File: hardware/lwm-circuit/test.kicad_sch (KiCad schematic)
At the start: 29 parts, among them J1 Analog, J2 Digital, J4 Micro_SD_Card_Det_Hirose_DM3AT, U1 MCP23017x-x-ML, U2 MCP23017x-x-ML, U3 MCP23017x-x-ML, U4 MCP23017x-x-ML, U5 MCP23017x-x-ML, U6 254

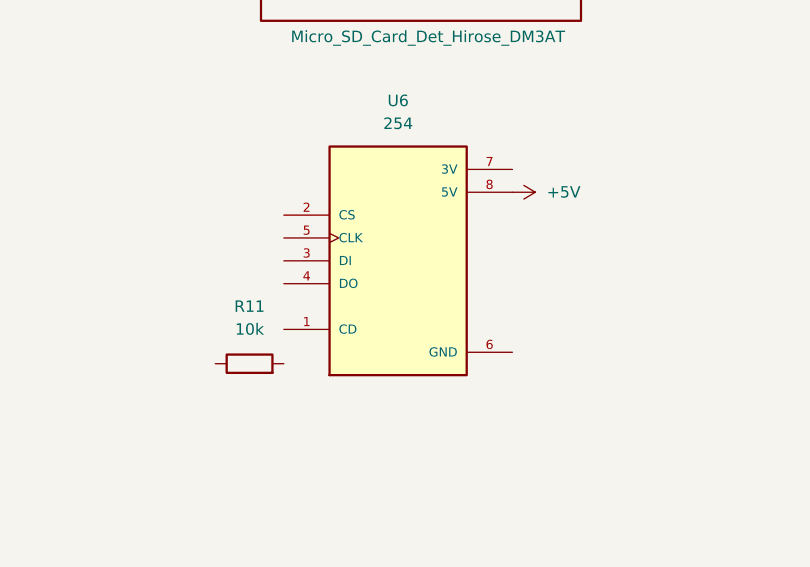
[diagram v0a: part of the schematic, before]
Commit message: rewired sd card
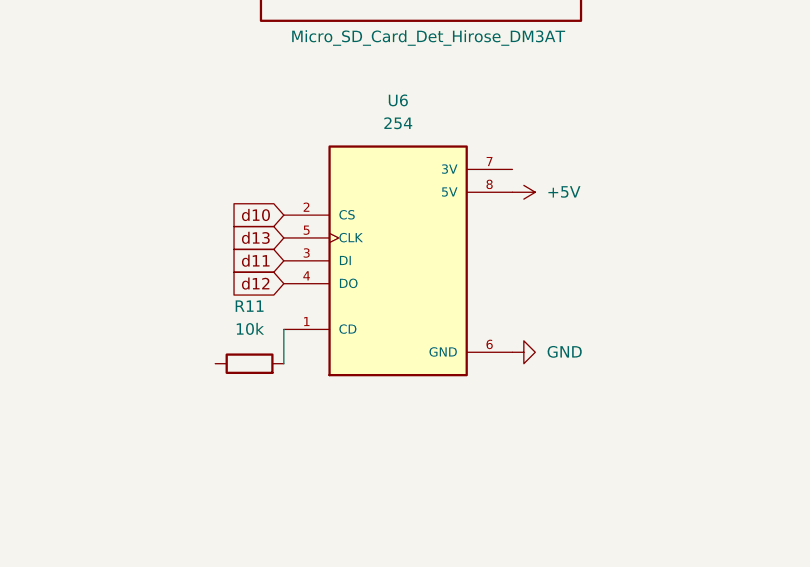
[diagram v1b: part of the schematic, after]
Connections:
- net GND: now also U6.6 (GND)
- net at U6.1 (CD): now also R11.2
- net d10: now reaches U6.2 (CS)
- net d11: now reaches U6.3 (DI)
- net d12: now reaches U6.4 (DO)
- net d13: now reaches U6.5 (CLK)
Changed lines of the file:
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@@
 	(wire
 		(pts
+			(xy 57.15 158.75) (xy 57.15 162.56)
+		)
+		(stroke
+			(width 0)
+			(type default)
+		)
+	)
+	(wire
+		(pts
 			(xy 24.13 20.32) (xy 135.89 20.32)
 		)
@@
 		)
 	)
+	(global_label "d11"
+		(shape input)
+		(at 57.15 151.13 180)
+		(fields_autoplaced yes)
+		(effects
+			(font
+				(size 1.27 1.27)
+			)
+			(justify right)
+		)
+		(property "Intersheetrefs" "${INTERSHEET_REFS}"
+			(at 53.8157 151.13 0)
+			(hide yes)
+			(show_name no)
+			(do_not_autoplace no)
+			(effects
+				(font
+					(size 1.27 1.27)
+				)
+				(justify right)
+			)
+		)
+	)
 	(global_label "R_1_DIAG"
 		(shape output)
@@
 		)
 	)
+	(global_label "d10"
+		(shape input)
+		(at 57.15 146.05 180)
+		(fields_autoplaced yes)
+		(effects
+			(font
+				(size 1.27 1.27)
+			)
+			(justify right)
+		)
+		(property "Intersheetrefs" "${INTERSHEET_REFS}"
+			(at 50.5017 146.05 0)
+			(hide yes)
+			(show_name no)
+			(do_not_autoplace no)
+			(effects
+				(font
+					(size 1.27 1.27)
+				)
+				(justify right)
+			)
+		)
+	)
 	(global_label "R_3_DIR"
 		(shape input)
@@
 		)
 	)
+	(global_label "d13"
+		(shape input)
+		(at 57.15 148.59 180)
+		(fields_autoplaced yes)
+		(effects
+			(font
+				(size 1.27 1.27)
+			)
+			(justify right)
+		)
+		(property "Intersheetrefs" "${INTERSHEET_REFS}"
+			(at 53.8157 148.59 0)
+			(hide yes)
+			(show_name no)
+			(do_not_autoplace no)
+			(effects
+				(font
+					(size 1.27 1.27)
+				)
+				(justify right)
+			)
+		)
+	)
 	(global_label "E_3_DIR"
 		(shape input)
@@
 		)
 	)
+	(global_label "d12"
+		(shape input)
+		(at 57.15 153.67 180)
+		(fields_autoplaced yes)
+		(effects
+			(font
+				(size 1.27 1.27)
+			)
+			(justify right)
+		)
+		(property "Intersheetrefs" "${INTERSHEET_REFS}"
+			(at 50.5017 153.67 0)
+			(hide yes)
+			(show_name no)
+			(do_not_autoplace no)
+			(effects
+				(font
+					(size 1.27 1.27)
+				)
+				(justify right)
+			)
+		)
+	)
 	(global_label "CS"
 		(shape input)
@@
 	)
 	(symbol
+		(lib_id "Device:R")
+		(at 53.34 162.56 90)
+		(unit 1)
+		(body_style 1)
+		(exclude_from_sim no)
+		(in_bom yes)
+		(on_board yes)
+		(in_pos_files yes)
+		(dnp no)
+		(fields_autoplaced yes)
+		(property "Reference" "R11"
+			(at 53.34 156.21 90)
+			(show_name no)
+			(do_not_autoplace no)
+			(effects
+				(font
+					(size 1.27 1.27)
+				)
+			)
+		)
+		(property "Value" "10k"
+			(at 53.34 158.75 90)
+			(show_name no)
+			(do_not_autoplace no)
+			(effects
+				(font
+					(size 1.27 1.27)
+				)
+			)
+		)
+		(property "Footprint" ""
+			(at 53.34 164.338 90)
+			(hide yes)
+			(show_name no)
+			(do_not_autoplace no)
+			(effects
+				(font
+					(size 1.27 1.27)
+				)
+			)
+		)
+		(property "Datasheet" ""
+			(at 53.34 162.56 0)
+			(hide yes)
+			(show_name no)
+			(do_not_autoplace no)
+			(effects
+				(font
+					(size 1.27 1.27)
+				)
+			)
+		)
+		(property "Description" "Resistor"
+			(at 53.34 162.56 0)
+			(hide yes)
+			(show_name no)
+			(do_not_autoplace no)
+			(effects
+				(font
+					(size 1.27 1.27)
+				)
+			)
+		)
+		(pin "1"
+		)
+		(pin "2"
+		)
+		(instances
+			(project "test"
+				(path "/0d35483a-0b12-46cc-b9f2-896fd6831779"
+					(reference "R11")
+					(unit 1)
+				)
+			)
+		)
+	)
+	(symbol
 		(lib_id "Adafruit TMC2209 Stepper Motor Driver-eagle-import:HEADER-1X1070MIL")
 		(at 171.45 210.82 90)
@@
 	)
 	(symbol
-		(lib_id "Device:R")
-		(at 53.34 162.56 90)
-		(unit 1)
-		(body_style 1)
-		(exclude_from_sim no)
-		(in_bom yes)
-		(on_board yes)
-		(in_pos_files yes)
-		(dnp no)
-		(fields_autoplaced yes)
-		(property "Reference" "R11"
-			(at 53.34 156.21 90)
-			(show_name no)
-			(do_not_autoplace no)
-			(effects
-				(font
-					(size 1.27 1.27)
-				)
-			)
-		)
-		(property "Value" "10k"
-			(at 53.34 158.75 90)
-			(show_name no)
-			(do_not_autoplace no)
-			(effects
-				(font
-					(size 1.27 1.27)
-				)
-			)
-		)
-		(property "Footprint" ""
-			(at 53.34 164.338 90)
-			(hide yes)
-			(show_name no)
-			(do_not_autoplace no)
-			(effects
-				(font
-					(size 1.27 1.27)
-				)
-			)
-		)
-		(property "Datasheet" ""
-			(at 53.34 162.56 0)
-			(hide yes)
-			(show_name no)
-			(do_not_autoplace no)
-			(effects
-				(font
-					(size 1.27 1.27)
-				)
-			)
-		)
-		(property "Description" "Resistor"
-			(at 53.34 162.56 0)
-			(hide yes)
-			(show_name no)
-			(do_not_autoplace no)
-			(effects
-				(font
-					(size 1.27 1.27)
-				)
-			)
-		)
-		(pin "1"
-		)
-		(pin "2"
-		)
-		(instances
-			(project "test"
-				(path "/0d35483a-0b12-46cc-b9f2-896fd6831779"
-					(reference "R11")
-					(unit 1)
-				)
-			)
-		)
-	)
-	(symbol
 		(lib_id "Interface_Expansion:MCP23017x-x-ML")
 		(at 454.66 53.34 0)
@@
 					(unit 1)
 				)
+			)
+		)
+	)
+	(symbol
+		(lib_id "power:GND")
+		(at 82.55 161.29 90)
+		(unit 1)
+		(body_style 1)
+		(exclude_from_sim no)
+		(in_bom yes)
+		(on_board yes)
+		(in_pos_files yes)
+		(dnp no)
+		(fields_autoplaced yes)
+		(property "Reference" "#PWR07"
+			(at 88.9 161.29 0)
+			(hide yes)
+			(show_name no)
+			(do_not_autoplace no)
+			(effects
+				(font
+					(size 1.27 1.27)
+				)
+			)
+		)
+		(property "Value" "GND"
+			(at 86.36 161.2899 90)
+			(show_name no)
+			(do_not_autoplace no)
+			(effects
+				(font
+					(size 1.27 1.27)
+				)
+				(justify right)
+			)
+		)
+		(property "Footprint" ""
+			(at 82.55 161.29 0)
+			(hide yes)
+			(show_name no)
+			(do_not_autoplace no)
+			(effects
+				(font
+					(size 1.27 1.27)
+				)
+			)
+		)
+		(property "Datasheet" ""
+			(at 82.55 161.29 0)
+			(hide yes)
+			(show_name no)
+			(do_not_autoplace no)
+			(effects
+				(font
+					(size 1.27 1.27)
+				)
+			)
+		)
+		(property "Description" "Power symbol creates a global label with name \"GND\" , ground"
+			(at 82.55 161.29 0)
+			(hide yes)
+			(show_name no)
+			(do_not_autoplace no)
+			(effects
+				(font
+					(size 1.27 1.27)
+				)
+			)
+		)
+		(pin "1"
+		)
+		(instances
+			(project "test"
+				(path "/0d35483a-0b12-46cc-b9f2-896fd6831779"
+					(reference "#PWR07")
+					(unit 1)
+				)

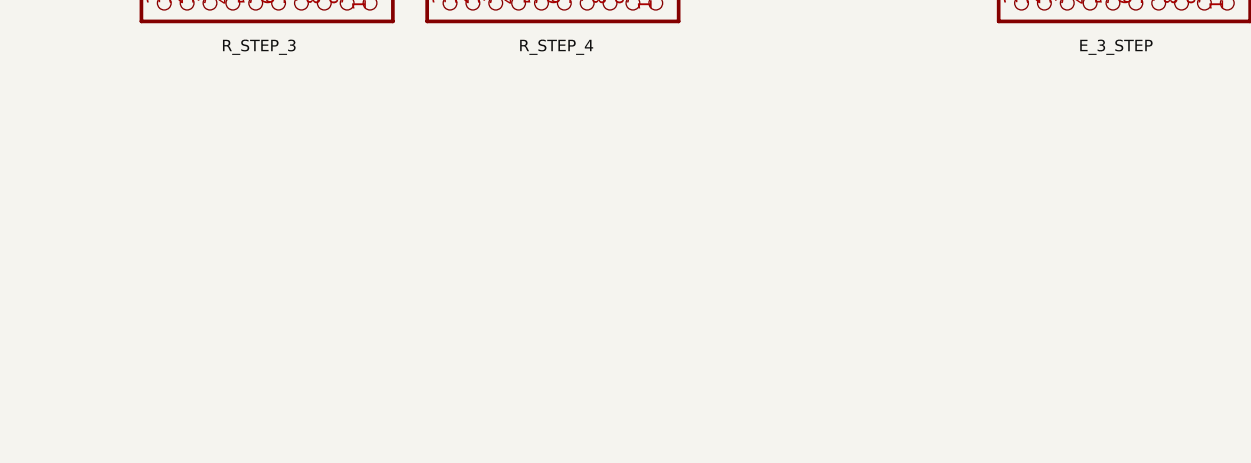
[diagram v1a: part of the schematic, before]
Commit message: added ultrasonic sensors
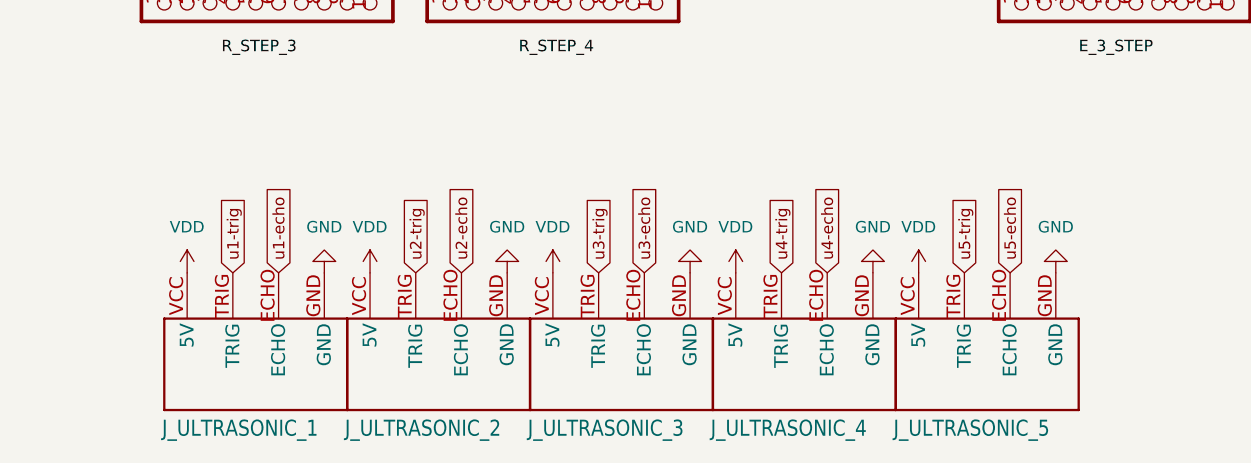
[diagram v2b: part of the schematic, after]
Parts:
- added J_ULTRASONIC_1, J_ULTRASONIC_2, J_ULTRASONIC_3, J_ULTRASONIC_4, J_ULTRASONIC_5: (no value), Ultrasonic Sensor HC-SR04:HC-SR04_FOOTPRINT, symbol Ultrasonic Sensor HC-SR04:HC-SR04
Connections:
- net GND: now also J_ULTRASONIC_1.GND, J_ULTRASONIC_2.GND, J_ULTRASONIC_3.GND, J_ULTRASONIC_4.GND, J_ULTRASONIC_5.GND
- net VDD: now also J_ULTRASONIC_1.VCC (5V), J_ULTRASONIC_2.VCC (5V), J_ULTRASONIC_3.VCC (5V), J_ULTRASONIC_4.VCC (5V), J_ULTRASONIC_5.VCC (5V)
- new net u1-echo: J_ULTRASONIC_1.ECHO
- new net u1-trig: J_ULTRASONIC_1.TRIG
- new net u2-echo: J_ULTRASONIC_2.ECHO
- new net u2-trig: J_ULTRASONIC_2.TRIG
- new net u3-echo: J_ULTRASONIC_3.ECHO
- new net u3-trig: J_ULTRASONIC_3.TRIG
- new net u4-echo: J_ULTRASONIC_4.ECHO
- new net u4-trig: J_ULTRASONIC_4.TRIG
- new net u5-echo: J_ULTRASONIC_5.ECHO
- new net u5-trig: J_ULTRASONIC_5.TRIG
